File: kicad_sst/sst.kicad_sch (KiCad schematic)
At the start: 35 parts

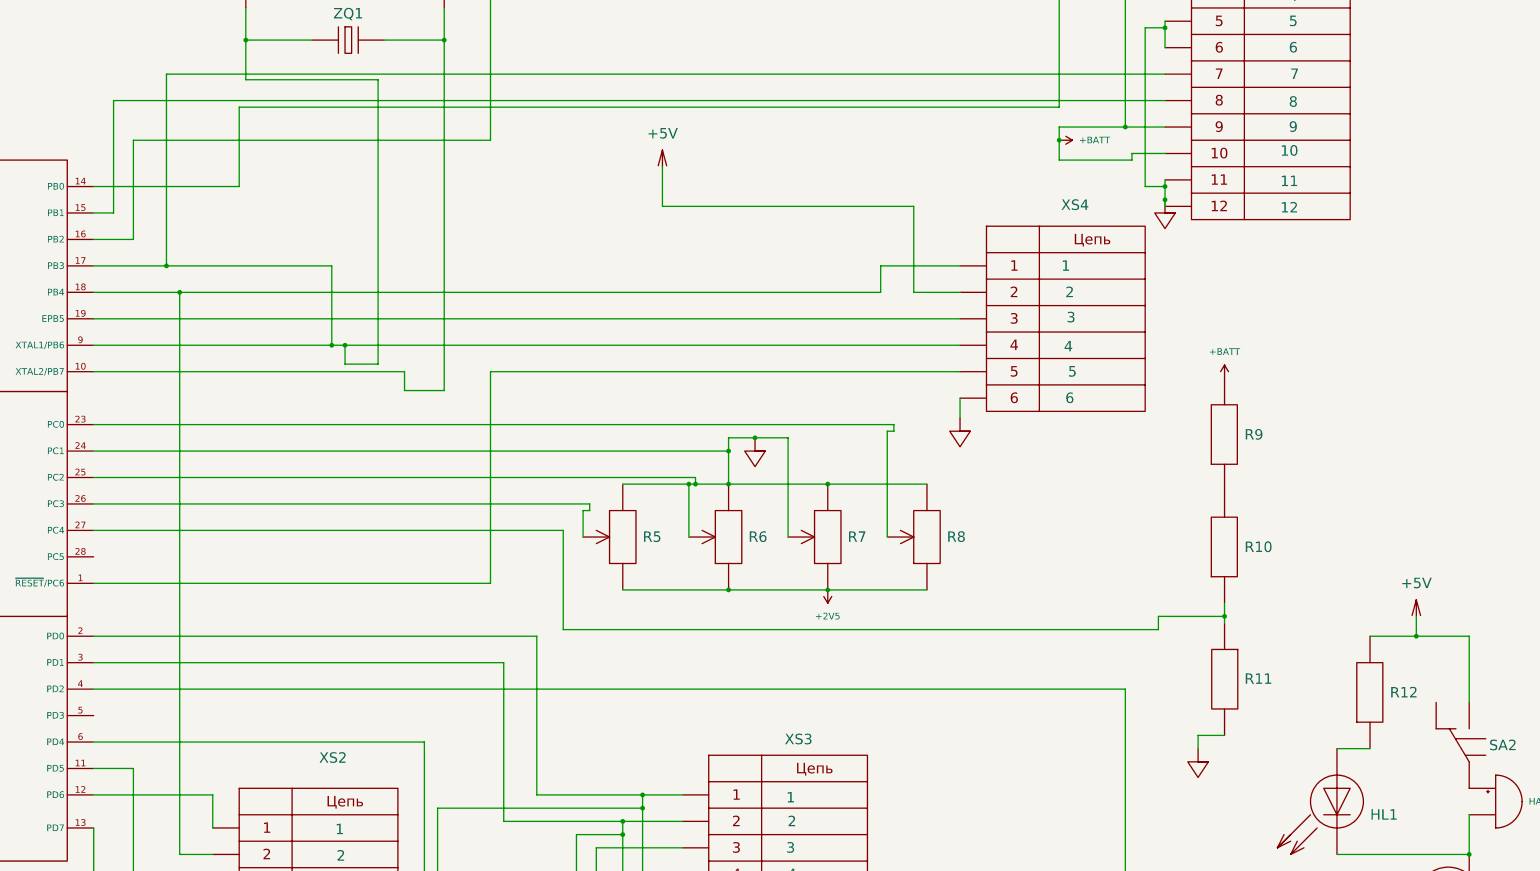
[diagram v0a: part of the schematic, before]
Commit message: fixes to potentiometers on schematics
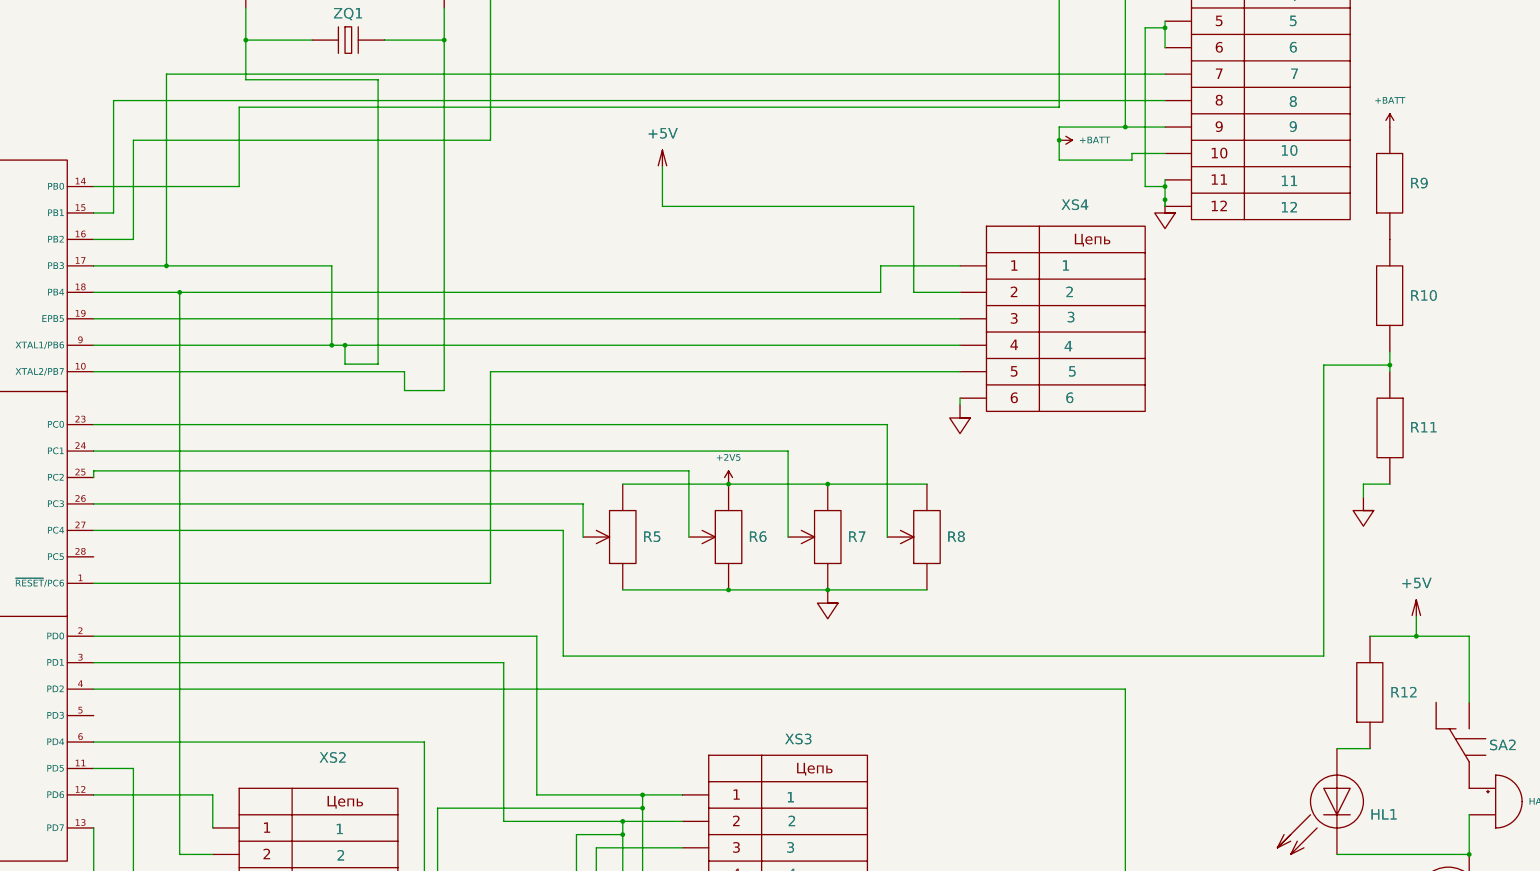
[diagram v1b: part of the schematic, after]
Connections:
- net +2V5: now also R5.3, R6.3, R7.3, R8.3; no longer R5.1, R6.1, R7.1, R8.1
- net GND: now also R5.1, R6.1, R7.1, R8.1; no longer DD1.24 (PC1), DD1.25 (PC2), R5.3, R6.2, R6.3, R7.2, R7.3, R8.3
- new net: DD1.24 (PC1), R7.2
- new net: DD1.25 (PC2), R6.2
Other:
- moved on the sheet: R10, R11, R9

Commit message: Changed capacitors
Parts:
- C5, C6: footprint Capacitor_THT:CP_Radial_D5.0mm_P2.50mm -> Capacitor_THT:C_Radial_D6.3mm_H5.0mm_P2.50mm
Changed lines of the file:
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@@
 			)
 		)
-		(property "Footprint" "Capacitor_THT:CP_Radial_D5.0mm_P2.50mm"
+		(property "Footprint" "Capacitor_THT:C_Radial_D6.3mm_H5.0mm_P2.50mm"
 			(at 159.258 33.688 0)
 			(effects
@@
 			)
 		)
-		(property "Footprint" "Capacitor_THT:CP_Radial_D5.0mm_P2.50mm"
+		(property "Footprint" "Capacitor_THT:C_Radial_D6.3mm_H5.0mm_P2.50mm"
 			(at 197.358 33.688 0)
 			(effects

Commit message: Подписал рамки
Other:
- title: (none) -> система тестирования\n сервоприводов\n квадрокоптера
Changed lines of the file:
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@@
 	(generator_version "8.0")
 	(paper "A3")
+	(title_block
+		(title "система тестирования\\n сервоприводов\\n квадрокоптера")
+		(date "2024-05-03")
+		(comment 1 "ГУИР 467993 013Э3")
+		(comment 2 "Корякин")
+	)
 	(junction
 		(at 386.08 160.02)
